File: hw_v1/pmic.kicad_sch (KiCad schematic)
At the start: 18 parts, among them U1 MCZ33810EK, U2 TC4424A, U3 TC4424A

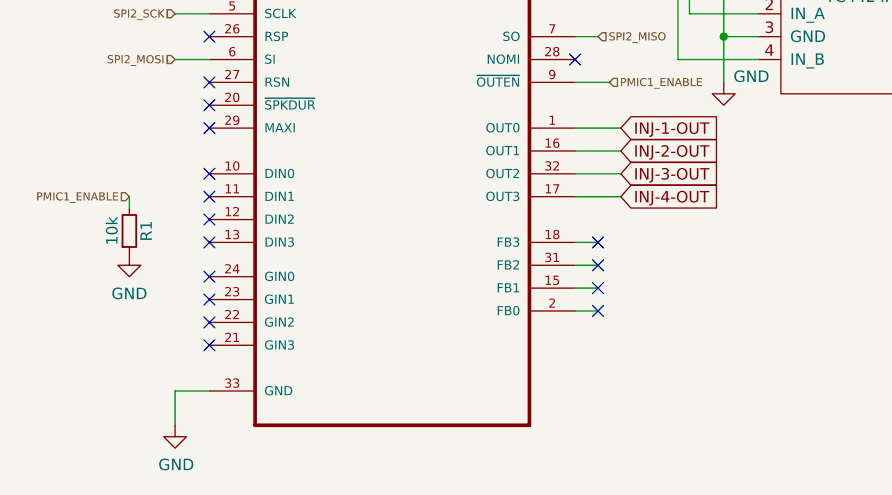
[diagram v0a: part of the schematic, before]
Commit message: add sensors/ relay ouputs, connect all IO to mcu
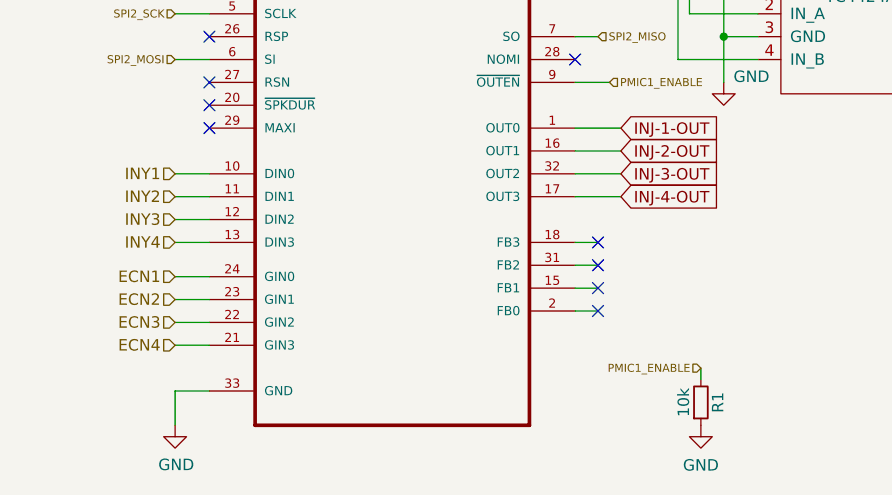
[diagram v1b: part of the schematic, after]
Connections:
- net INY1: now reaches U1.10 (DIN0)
- net INY2: now reaches U1.11 (DIN1)
- net INY3: now reaches U1.12 (DIN2)
- net INY4: now reaches U1.13 (DIN3)
- net ECN4: now reaches U1.21 (GIN3)
- net ECN3: now reaches U1.22 (GIN2)
- net ECN2: now reaches U1.23 (GIN1)
- net ECN1: now reaches U1.24 (GIN0)
- no-connect marks 17 -> 9
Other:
- company: (none) -> Churrosoft ®
- title: (none) -> μEFI (Speeduino FW compatible)
- moved on the sheet: R1
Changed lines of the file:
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@@
 	(generator_version "7.99")
 	(paper "A4")
+	(title_block
+		(title "μEFI (Speeduino FW compatible)")
+		(date "2023-12-25")
+		(rev "v6")
+		(company "Churrosoft ®")
+		(comment 1 "CERN-OHL-S-2.0 license\n")
+	)
 	(junction
 		(at 107.95 93.98)
@@
 	)
 	(no_connect
-		(at 50.8 120.65)
-	)
-	(no_connect
-		(at 50.8 111.76)
-	)
-	(no_connect
 		(at 93.98 121.92)
-	)
-	(no_connect
-		(at 50.8 114.3)
 	)
 	(no_connect
@@
 	)
 	(no_connect
-		(at 50.8 123.19)
-	)
-	(no_connect
-		(at 50.8 128.27)
-	)
-	(no_connect
 		(at 91.44 96.52)
-	)
-	(no_connect
-		(at 50.8 109.22)
 	)
 	(no_connect
@@
 		(at 93.98 124.46)
 	)
-	(no_connect
-		(at 50.8 116.84)
-	)
-	(no_connect
-		(at 50.8 125.73)
-	)
 	(wire
 		(pts
@@
 	(wire
 		(pts
+			(xy 46.99 125.73) (xy 50.8 125.73)
+		)
+		(stroke
+			(width 0)
+			(type default)
+		)
+	)
+	(wire
+		(pts
 			(xy 135.89 74.93) (xy 139.7 74.93)
 		)
@@
 	(wire
 		(pts
+			(xy 46.99 123.19) (xy 50.8 123.19)
+		)
+		(stroke
+			(width 0)
+			(type default)
+		)
+	)
+	(wire
+		(pts
 			(xy 251.46 85.09) (xy 251.46 82.55)
 		)
@@
 	(wire
 		(pts
+			(xy 46.99 111.76) (xy 50.8 111.76)
+		)
+		(stroke
+			(width 0)
+			(type default)
+		)
+	)
+	(wire
+		(pts
 			(xy 91.44 83.82) (xy 104.14 83.82)
 		)
@@
 	(wire
 		(pts
+			(xy 46.99 109.22) (xy 50.8 109.22)
+		)
+		(stroke
+			(width 0)
+			(type default)
+		)
+	)
+	(wire
+		(pts
 			(xy 247.65 80.01) (xy 251.46 80.01)
 		)
@@
 	(wire
 		(pts
+			(xy 46.99 128.27) (xy 50.8 128.27)
+		)
+		(stroke
+			(width 0)
+			(type default)
+		)
+	)
+	(wire
+		(pts
 			(xy 46.99 137.16) (xy 46.99 133.35)
 		)
@@
 	(wire
 		(pts
+			(xy 46.99 116.84) (xy 50.8 116.84)
+		)
+		(stroke
+			(width 0)
+			(type default)
+		)
+	)
+	(wire
+		(pts
 			(xy 91.44 116.84) (xy 93.98 116.84)
 		)
@@
 	(wire
 		(pts
-			(xy 41.91 111.76) (xy 41.91 113.03)
+			(xy 105.41 130.81) (xy 105.41 132.08)
 		)
 		(stroke
@@
 	(wire
 		(pts
+			(xy 46.99 114.3) (xy 50.8 114.3)
+		)
+		(stroke
+			(width 0)
+			(type default)
+		)
+	)
+	(wire
+		(pts
 			(xy 107.95 99.06) (xy 107.95 93.98)
 		)
@@
 			(width 0)
 			(type solid)
+		)
+	)
+	(wire
+		(pts
+			(xy 46.99 120.65) (xy 50.8 120.65)
+		)
+		(stroke
+			(width 0)
+			(type default)
 		)
 	)
@@
 		)
 	)
+	(hierarchical_label "INY3"
+		(shape input)
+		(at 46.99 114.3 180)
+		(fields_autoplaced yes)
+		(effects
+			(font
+				(size 1.27 1.27)
+			)
+			(justify right)
+		)
+	)
 	(hierarchical_label "PMIC1_ENABLE"
 		(shape input)
-		(at 41.91 111.76 180)
+		(at 105.41 130.81 180)
 		(fields_autoplaced yes)
 		(effects
 			(font
 				(size 0.889 0.889)
+			)
+			(justify right)
+		)
+	)
+	(hierarchical_label "ECN1"
+		(shape input)
+		(at 46.99 120.65 180)
+		(fields_autoplaced yes)
+		(effects
+			(font
+				(size 1.27 1.27)
+			)
+			(justify right)
+		)
+	)
+	(hierarchical_label "ECN4"
+		(shape input)
+		(at 46.99 128.27 180)
+		(fields_autoplaced yes)
+		(effects
+			(font
+				(size 1.27 1.27)
+			)
+			(justify right)
+		)
+	)
+	(hierarchical_label "ECN3"
+		(shape input)
+		(at 46.99 125.73 180)
+		(fields_autoplaced yes)
+		(effects
+			(font
+				(size 1.27 1.27)
 			)
 			(justify right)
@@
 		)
 	)
+	(hierarchical_label "ECN2"
+		(shape input)
+		(at 46.99 123.19 180)
+		(fields_autoplaced yes)
+		(effects
+			(font
+				(size 1.27 1.27)
+			)
+			(justify right)
+		)
+	)
+	(hierarchical_label "INY1"
+		(shape input)
+		(at 46.99 109.22 180)
+		(fields_autoplaced yes)
+		(effects
+			(font
+				(size 1.27 1.27)
+			)
+			(justify right)
+		)
+	)
 	(hierarchical_label "PMIC1_ENABLE"
 		(shape input)
@@
 			)
 			(justify left)
+		)
+	)
+	(hierarchical_label "INY4"
+		(shape input)
+		(at 46.99 116.84 180)
+		(fields_autoplaced yes)
+		(effects
+			(font
+				(size 1.27 1.27)
+			)
+			(justify right)
+		)
+	)
+	(hierarchical_label "INY2"
+		(shape input)
+		(at 46.99 111.76 180)
+		(fields_autoplaced yes)
+		(effects
+			(font
+				(size 1.27 1.27)
+			)
+			(justify right)
 		)
 	)
@@
 	(symbol
 		(lib_id "Device:R_Small")
-		(at 41.91 115.57 0)
+		(at 105.41 134.62 0)
 		(mirror x)
 		(unit 1)
@@
 		(dnp no)
 		(property "Reference" "R1"
-			(at 43.815 115.57 90)
+			(at 107.315 134.62 90)
 			(effects
 				(font
@@
 		)
 		(property "Value" "10k"
-			(at 40.005 115.57 90)
+			(at 103.505 134.62 90)
 			(effects
 				(font
@@
 		)
 		(property "Footprint" "Resistor_SMD:R_0805_2012Metric"
-			(at 41.91 115.57 0)
+			(at 105.41 134.62 0)
 			(effects
 				(font
@@
 		)
 		(property "Datasheet" "~"
-			(at 41.91 115.57 0)
+			(at 105.41 134.62 0)
 			(effects
 				(font
@@
 		)
 		(property "Description" ""
-			(at 41.91 115.57 0)
+			(at 105.41 134.62 0)
 			(effects
 				(font
@@
 		)
 		(property "LCSC" "C17414"
-			(at 41.91 115.57 90)
+			(at 105.41 134.62 90)
 			(effects
 				(font
@@
 		(lib_name "GND_1")
 		(lib_id "power:GND")
-		(at 41.91 118.11 0)
+		(at 105.41 137.16 0)
 		(unit 1)
 		(exclude_from_sim no)
@@
 		(dnp no)
 		(property "Reference" "#PWR02"
-			(at 41.91 124.46 0)
+			(at 105.41 143.51 0)
 			(effects
 				(font
@@
 		)
 		(property "Value" "GND"
-			(at 41.91 122.555 0)
+			(at 105.41 141.605 0)
 			(effects
 				(font
@@
 		)
 		(property "Footprint" ""
-			(at 41.91 118.11 0)
+			(at 105.41 137.16 0)
 			(effects
 				(font
@@
 		)
 		(property "Datasheet" ""
-			(at 41.91 118.11 0)
+			(at 105.41 137.16 0)
 			(effects
 				(font
@@
 		)
 		(property "Description" ""
-			(at 41.91 118.11 0)
-			(effects
-				(font
+			(at 105.41 137.16 0)
+			(effects
+				(font

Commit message: wip pcb layout
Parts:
- U1: footprint Library:SOP65P1030X245-33N -> uEFI_v5:SOP65P1030X245-33N
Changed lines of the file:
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@@
 			)
 		)
-		(property "Footprint" "Library:SOP65P1030X245-33N"
+		(property "Footprint" "uEFI_v5:SOP65P1030X245-33N"
 			(at 71.755 100.965 0)
 			(effects

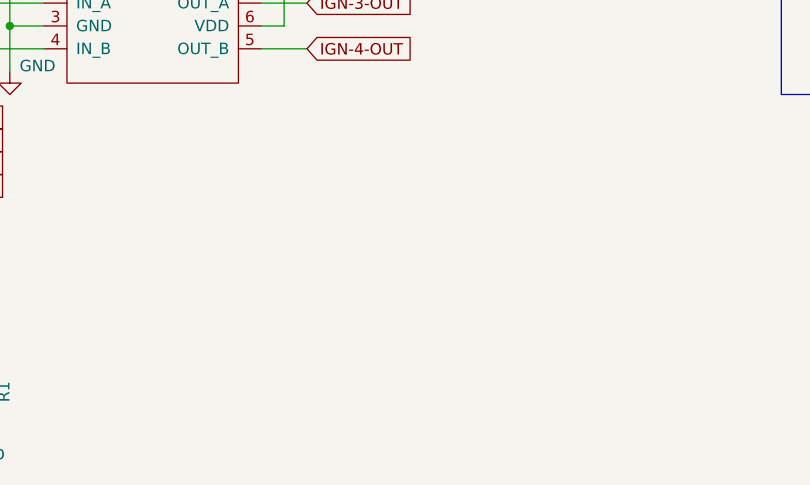
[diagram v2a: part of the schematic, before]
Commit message: placed al SMD, wip pmic traces
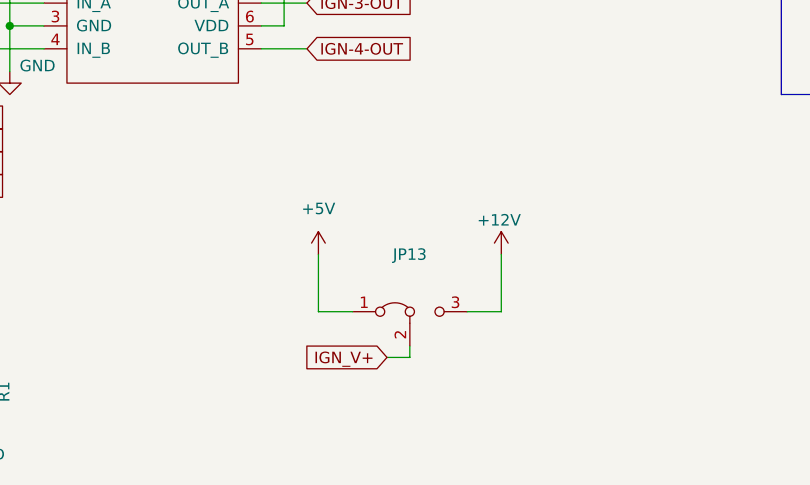
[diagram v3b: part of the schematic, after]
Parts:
- added JP13: Jumper_3_Bridged12, Jumper:SolderJumper-3_P1.3mm_Bridged2Bar12_Pad1.0x1.5mm, symbol Jumper:Jumper_3_Bridged12
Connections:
- net +12V: now also JP13.3 (B)
- net IGN_V+: now also JP13.2 (C)
- new net +5V: JP13.1 (A)

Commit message: update SD card holder to Molex 47352
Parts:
- JP13: now left out of the parts list
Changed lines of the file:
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@@
 	(version 20231120)
 	(generator "eeschema")
-	(generator_version "7.99")
+	(generator_version "8.0")
 	(paper "A4")
 	(title_block
 		(title "μEFI (Speeduino FW compatible)")
 		(date "2023-12-25")
-		(rev "v6")
+		(rev "v6.1")
 		(company "Churrosoft ®")
-		(comment 1 "CERN-OHL-S-2.0 license\n")
+		(comment 1 "CERN-OHL-S-2.0 license")
 	)
 	(junction
@@
 		(unit 1)
 		(exclude_from_sim no)
-		(in_bom yes)
+		(in_bom no)
 		(on_board yes)
 		(dnp no)

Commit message: update footprints
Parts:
- D11, D3, D6, D8: value D -> 1N4148; footprint Diode_SMD:D_SOD-323_HandSoldering -> Diode_SMD:D_SOD-523
- R1: footprint Resistor_SMD:R_0805_2012Metric -> Resistor_SMD:R_0603_1608Metric; LCSC C17414 -> C115324
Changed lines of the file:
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@@
 			)
 		)
-		(property "Footprint" "Resistor_SMD:R_0805_2012Metric"
+		(property "Footprint" "Resistor_SMD:R_0603_1608Metric"
 			(at 105.41 134.62 0)
 			(effects
@@
 			)
 		)
-		(property "LCSC" "C17414"
+		(property "LCSC" "C115324"
 			(at 105.41 134.62 90)
 			(effects
@@
 			)
 		)
-		(property "Value" "D"
+		(property "Value" "1N4148"
 			(at 241.3 40.005 0)
 			(effects
@@
 			)
 		)
-		(property "Footprint" "Diode_SMD:D_SOD-323_HandSoldering"
+		(property "Footprint" "Diode_SMD:D_SOD-523"
 			(at 236.855 63.5 0)
 			(effects
@@
 			)
 		)
-		(property "Value" "D"
+		(property "Value" "1N4148"
 			(at 241.3 42.545 0)
 			(effects
@@
 			)
 		)
-		(property "Footprint" "Diode_SMD:D_SOD-323_HandSoldering"
+		(property "Footprint" "Diode_SMD:D_SOD-523"
 			(at 236.855 66.04 0)
 			(effects
@@
 			)
 		)
-		(property "Value" "D"
+		(property "Value" "1N4148"
 			(at 241.3 34.925 0)
 			(effects
@@
 			)
 		)
-		(property "Footprint" "Diode_SMD:D_SOD-323_HandSoldering"
+		(property "Footprint" "Diode_SMD:D_SOD-523"
 			(at 236.855 58.42 0)
 			(effects
@@
 			)
 		)
-		(property "Value" "D"
+		(property "Value" "1N4148"
 			(at 241.3 37.465 0)
 			(effects
@@
 			)
 		)
-		(property "Footprint" "Diode_SMD:D_SOD-323_HandSoldering"
+		(property "Footprint" "Diode_SMD:D_SOD-523"
 			(at 236.855 60.96 0)
 			(effects

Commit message: update from inventree
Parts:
- D11, D3, D6, D8: value 1N4148 -> 1N5819WS; footprint Diode_SMD:D_SOD-523 -> Diode_SMD:D_SOD-323_HandSoldering; LCSC C5277952 -> C191023; STOCK (none) -> DIO-000272-00
- JP13: now not fitted
- R1: STOCK (none) -> RES-000118-00
- RN1, RN2: STOCK (none) -> RES-000353-00
- U1: LCSC (none) -> -; STOCK (none) -> PWR-000021-00
- U2, U3: STOCK (none) -> ICS-000345-00
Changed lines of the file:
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@@
 		(in_bom no)
 		(on_board yes)
-		(dnp no)
+		(dnp yes)
 		(fields_autoplaced yes)
 		(property "Reference" "JP13"
@@
 				(font
 					(size 0.889 0.889)
+				)
+				(hide yes)
+			)
+		)
+		(property "STOCK" "ICS-000345-00"
+			(at 139.7 121.92 0)
+			(effects
+				(font
+					(size 1.27 1.27)
 				)
 				(hide yes)
@@
 			)
 		)
+		(property "STOCK" "RES-000118-00"
+			(at 105.41 134.62 0)
+			(effects
+				(font
+					(size 1.27 1.27)
+				)
+				(hide yes)
+			)
+		)
 		(pin "1"
 		)
@@
 			)
 		)
+		(property "STOCK" "ICS-000345-00"
+			(at 139.7 105.41 0)
+			(effects
+				(font
+					(size 1.27 1.27)
+				)
+				(hide yes)
+			)
+		)
 		(pin "1"
 		)
@@
 			)
 		)
-		(property "Value" "1N4148"
+		(property "Value" "1N5819WS"
 			(at 241.3 40.005 0)
 			(effects
@@
 			)
 		)
-		(property "Footprint" "Diode_SMD:D_SOD-523"
+		(property "Footprint" "Diode_SMD:D_SOD-323_HandSoldering"
 			(at 236.855 63.5 0)
 			(effects
@@
 			)
 		)
-		(property "LCSC" "C5277952"
+		(property "LCSC" "C191023"
 			(at 241.3 43.18 0)
 			(effects
 				(font
 					(size 0.889 0.889)
+				)
+				(hide yes)
+			)
+		)
+		(property "STOCK" "DIO-000272-00"
+			(at 241.3 43.18 0)
+			(effects
+				(font
+					(size 1.27 1.27)
 				)
 				(hide yes)
@@
 			)
 		)
-		(property "Value" "1N4148"
+		(property "Value" "1N5819WS"
 			(at 241.3 42.545 0)
 			(effects
@@
 			)
 		)
-		(property "Footprint" "Diode_SMD:D_SOD-523"
+		(property "Footprint" "Diode_SMD:D_SOD-323_HandSoldering"
 			(at 236.855 66.04 0)
 			(effects
@@
 			)
 		)
-		(property "LCSC" "C5277952"
+		(property "LCSC" "C191023"
 			(at 241.3 45.72 0)
 			(effects
 				(font
 					(size 0.889 0.889)
+				)
+				(hide yes)
+			)
+		)
+		(property "STOCK" "DIO-000272-00"
+			(at 241.3 45.72 0)
+			(effects
+				(font
+					(size 1.27 1.27)
 				)
 				(hide yes)
@@
 			)
 		)
-		(property "Value" "1N4148"
+		(property "Value" "1N5819WS"
 			(at 241.3 34.925 0)
 			(effects
@@
 			)
 		)
-		(property "Footprint" "Diode_SMD:D_SOD-523"
+		(property "Footprint" "Diode_SMD:D_SOD-323_HandSoldering"
 			(at 236.855 58.42 0)
 			(effects
@@
 			)
 		)
-		(property "LCSC" "C5277952"
+		(property "LCSC" "C191023"
 			(at 241.3 38.1 0)
 			(effects
 				(font
 					(size 0.889 0.889)
+				)
+				(hide yes)
+			)
+		)
+		(property "STOCK" "DIO-000272-00"
+			(at 241.3 38.1 0)
+			(effects
+				(font
+					(size 1.27 1.27)
 				)
 				(hide yes)
@@
 			)
 		)
-		(property "Value" "1N4148"
+		(property "Value" "1N5819WS"
 			(at 241.3 37.465 0)
 			(effects
@@
 			)
 		)
-		(property "Footprint" "Diode_SMD:D_SOD-523"
+		(property "Footprint" "Diode_SMD:D_SOD-323_HandSoldering"
 			(at 236.855 60.96 0)
 			(effects
@@
 			)
 		)
-		(property "LCSC" "C5277952"
+		(property "LCSC" "C191023"
 			(at 241.3 40.64 0)
 			(effects
 				(font
 					(size 0.889 0.889)
+				)
+				(hide yes)
+			)
+		)
+		(property "STOCK" "DIO-000272-00"
+			(at 241.3 40.64 0)
+			(effects
+				(font
+					(size 1.27 1.27)
 				)
 				(hide yes)
@@
 			)
 		)
+		(property "STOCK" "RES-000353-00"
+			(at 233.68 80.01 0)
+			(effects
+				(font
+					(size 1.27 1.27)
+				)
+				(hide yes)
+			)
+		)
 		(pin "1"
 		)
@@
 				)
 				(justify left bottom)
+				(hide yes)
+			)
+		)
+		(property "LCSC" "-"
+			(at 71.755 100.965 0)
+			(effects
+				(font
+					(size 1.27 1.27)
+				)
+				(hide yes)
+			)
+		)
+		(property "STOCK" "PWR-000021-00"
+			(at 71.755 100.965 0)
+			(effects
+				(font
+					(size 1.27 1.27)
+				)
 				(hide yes)
 			)
@@
 				)
 				(hide yes)
+			)
+		)
+		(property "STOCK" "RES-000353-00"
+			(at 220.98 40.64 0)
+			(effects
+				(font
+					(size 1.27 1.27)
+				)
+				(hide yes)
